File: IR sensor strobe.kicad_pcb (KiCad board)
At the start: 2 copper layers, 37.5 x 43.5 mm, 22 parts, among them J1 CTL, J2 Sensors, J3 Conn_01x05, J4 Conn_01x02, Q1 NPN, Q2 OP550, Q3 OP550, Q4 OP550, Q5 OP550

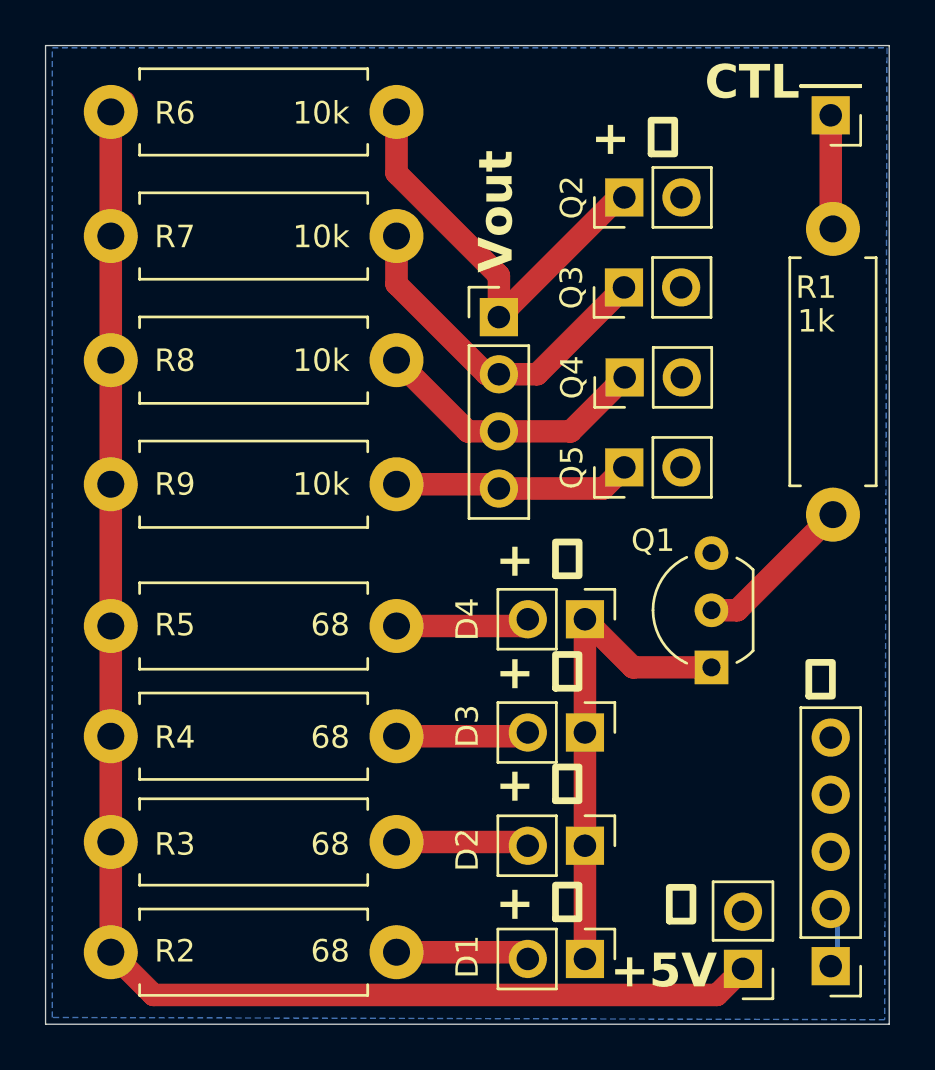
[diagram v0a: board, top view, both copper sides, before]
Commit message: Add supply decoupling and CTL pull-down; move emitters/detectors off-board
Schematic and README work predating the oscillator change:

- Add C1 (10 uF) and C2 (0.1 uF) across the +5 V / GND entry at J4 to
  absorb the ~200 mA switching transient of the emitter array.
- Add R10 (10k) pull-down on CTL so the emitter array stays dark when
  CTL is undriven.
- D1-D4 (OP140) and Q2-Q5 (OP550) carry no footprints; they are remote
  parts wired through J5-J8. PCB nets renamed accordingly.
- README updated to match.

INCONSISTENT SNAPSHOT -- this revision is not a coherent design state.

The .kicad_pcb captured here had already been re-imported from the
*later* schematic, so it contains U1, R11, R12, C3-C5 and the DIN0207
resistor footprints, none of which exist in the .kicad_sch at this
commit. The schematic and board therefore disagree.

Do not build from, bisect to, or generate fabrication outputs from this
revision. The last coherent state before this work is 10a3dae; the next
coherent state is the following commit ("Add on-board 500 Hz strobe
oscillator; fix Q1 pinout; shrink resistors") and everything after it.
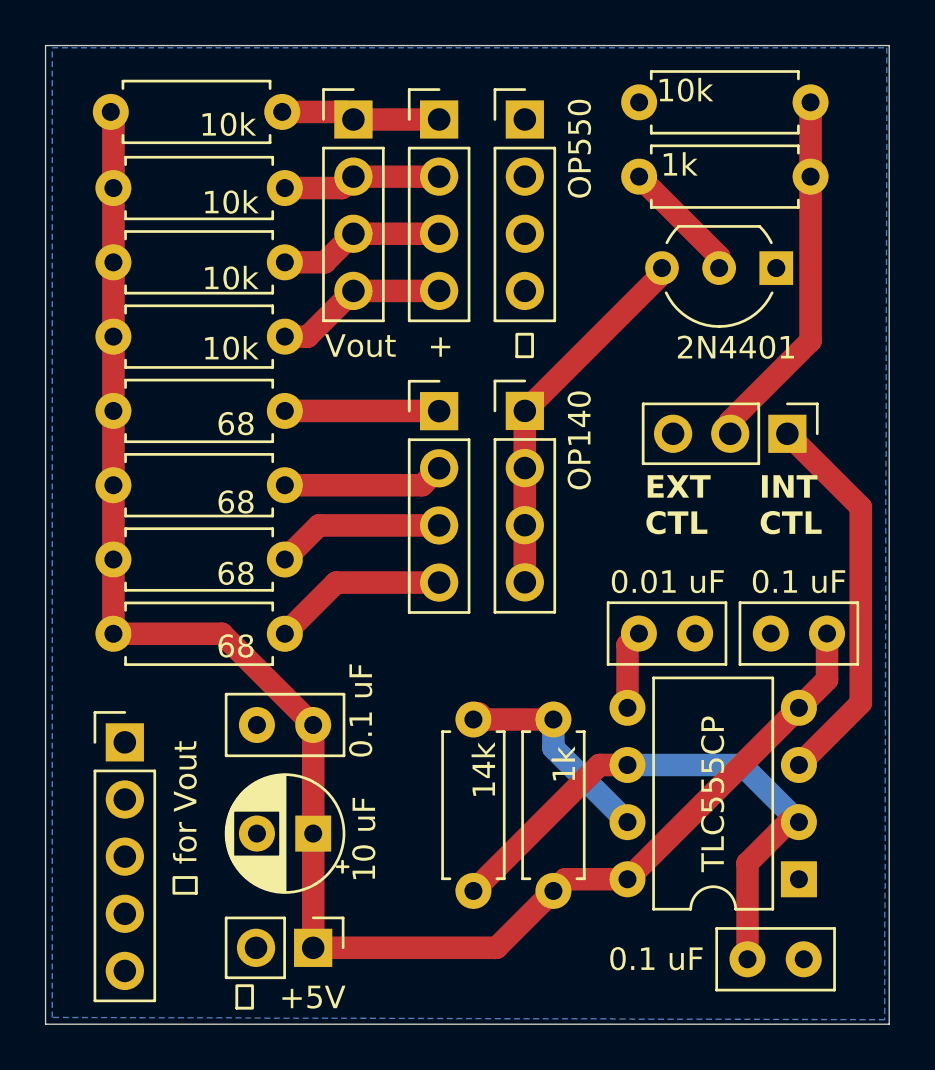
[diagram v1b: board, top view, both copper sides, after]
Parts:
- removed D1, D2, D3, D4: OP140, Connector_PinHeader_2.54mm:PinHeader_1x02_P2.54mm_Vertical
- removed Q2, Q3, Q4, Q5: OP550, Connector_PinHeader_2.54mm:PinHeader_1x02_P2.54mm_Vertical
- added C1: 10 uF, Capacitor_THT:CP_Radial_D5.0mm_P2.50mm, F.Cu at (73.4, 97.5)
- added C2: 0.1 uF, Capacitor_THT:C_Disc_D5.0mm_W2.5mm_P2.50mm, F.Cu at (73.4, 92.7)
- added C3: 0.1 uF, Capacitor_THT:C_Disc_D5.0mm_W2.5mm_P2.50mm, F.Cu at (92.7, 103.1)
- added C4: 0.01 uF, Capacitor_THT:C_Disc_D5.0mm_W2.5mm_P2.50mm, F.Cu at (87.9, 88.6)
- added C5: 0.1 uF, Capacitor_THT:C_Disc_D5.0mm_W2.5mm_P2.50mm, F.Cu at (96.2, 88.6)
- added J5: OP550 return, Connector_PinHeader_2.54mm:PinHeader_1x04_P2.54mm_Vertical, F.Cu at (82.8, 65.8)
- added J6: OP550 out, Connector_PinHeader_2.54mm:PinHeader_1x04_P2.54mm_Vertical, F.Cu at (79.0, 65.8)
- added J7: OP140 in, Connector_PinHeader_2.54mm:PinHeader_1x04_P2.54mm_Vertical, F.Cu at (82.8, 78.7)
- added J8: OP140 out, Connector_PinHeader_2.54mm:PinHeader_1x04_P2.54mm_Vertical, F.Cu at (79.0, 78.8)
- added R10: 10k, Resistor_THT:R_Axial_DIN0207_L6.3mm_D2.5mm_P7.62mm_Horizontal, F.Cu at (95.5, 65.0)
- added R11: 1k, Resistor_THT:R_Axial_DIN0207_L6.3mm_D2.5mm_P7.62mm_Horizontal, F.Cu at (84.1, 100.1)
- added R12: 14k, Resistor_THT:R_Axial_DIN0207_L6.3mm_D2.5mm_P7.62mm_Horizontal, F.Cu at (80.5, 92.5)
- added U1: TLC555CP, Package_DIP:DIP-8_W7.62mm, F.Cu at (95.0, 99.6)
- J1: value CTL -> CTL select; footprint Connector_PinHeader_2.54mm:PinHeader_1x01_P2.54mm_Vertical -> Connector_PinHeader_2.54mm:PinHeader_1x03_P2.54mm_Vertical
- Q1: value NPN -> 2N4401
- R1, R2, R3, R4, R5, R6, R7, R8, R9: footprint Resistor_THT:R_Axial_DIN0411_L9.9mm_D3.6mm_P12.70mm_Horizontal -> Resistor_THT:R_Axial_DIN0207_L6.3mm_D2.5mm_P7.62mm_Horizontal
- moved J3 32.9 mm to (65.0, 93.5), turned to 0 degrees
- moved J4 19.1 mm to (73.4, 102.6), turned to -90 degrees
- moved Q1 18.0 mm to (94.0, 72.4), turned to 180 degrees
- moved R1 17.3 mm to (87.9, 68.3), turned to 0 degrees
- moved J1 14.3 mm to (94.5, 79.8), turned to -90 degrees
- moved R2 14.2 mm to (64.5, 88.6)
- moved R3 12.6 mm to (64.5, 85.3)
- moved R4 11.2 mm to (64.5, 82.0)
- moved J2 10.9 mm to (75.2, 65.8)
- moved R5 9.56 mm to (64.5, 78.7)
- moved R9 6.56 mm to (64.5, 75.4)
- moved R8 4.35 mm to (64.5, 72.1)
- moved R7 2.14 mm to (64.5, 68.8)
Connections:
- J1 pad 1: Net-(J1-Pin_1) -> /OSC
- Q1 pad 1: Net-(D1-K) -> GND
- Q1 pad 3: GND -> Net-(J7-Pin_1)
- R1 pad 2: Net-(J1-Pin_1) -> Net-(J1-Pin_2)
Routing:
- net Net-(U1-THR): track 0.00 -> 25.2 mm
- net Net-(D1-K): track 21.6 -> 0.00 mm
- net /OSC: track 0.00 -> 17.2 mm
- net Net-(J7-Pin_1): track 0.00 -> 16.9 mm
- net Net-(J1-Pin_2): track 0.00 -> 16.2 mm
- net Net-(J2-Pin_1): track 18.8 -> 7.11 mm
- net Net-(U1-DIS): track 0.00 -> 9.71 mm
- net Net-(J2-Pin_2): track 15.5 -> 7.07 mm
- net +5V: track 67.5 -> 74.1 mm
- net Net-(J1-Pin_1): track 5.09 -> 0.00 mm
- net Net-(J2-Pin_3): track 12.4 -> 7.38 mm
- net Net-(U1-CV): track 0.00 -> 3.51 mm
- net Net-(J2-Pin_4): track 10.6 -> 7.70 mm
- net GND: track 2.64 -> 0.00 mm
- net Net-(J8-Pin_4): track 5.96 -> 7.80 mm
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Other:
- board text added: "+"
- board text added: "EXT CTL"
- board text added: "INT CTL"
- board text added: "OP140"
- board text added: "OP550"
- board text added: "Strobed IR emitter/sensor w/ internal generator 2026.09.14 Brad Buran"
- board text added: "⏚ for Vout"
- board text removed: "+ ⏚"
- board text removed: "CTL"
- board text removed: "Strobed IR emitter/sensor 2026.02.17 Brad Buran"
